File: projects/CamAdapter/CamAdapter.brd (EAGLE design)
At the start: 25.4 x 41.9 mm, 5 parts

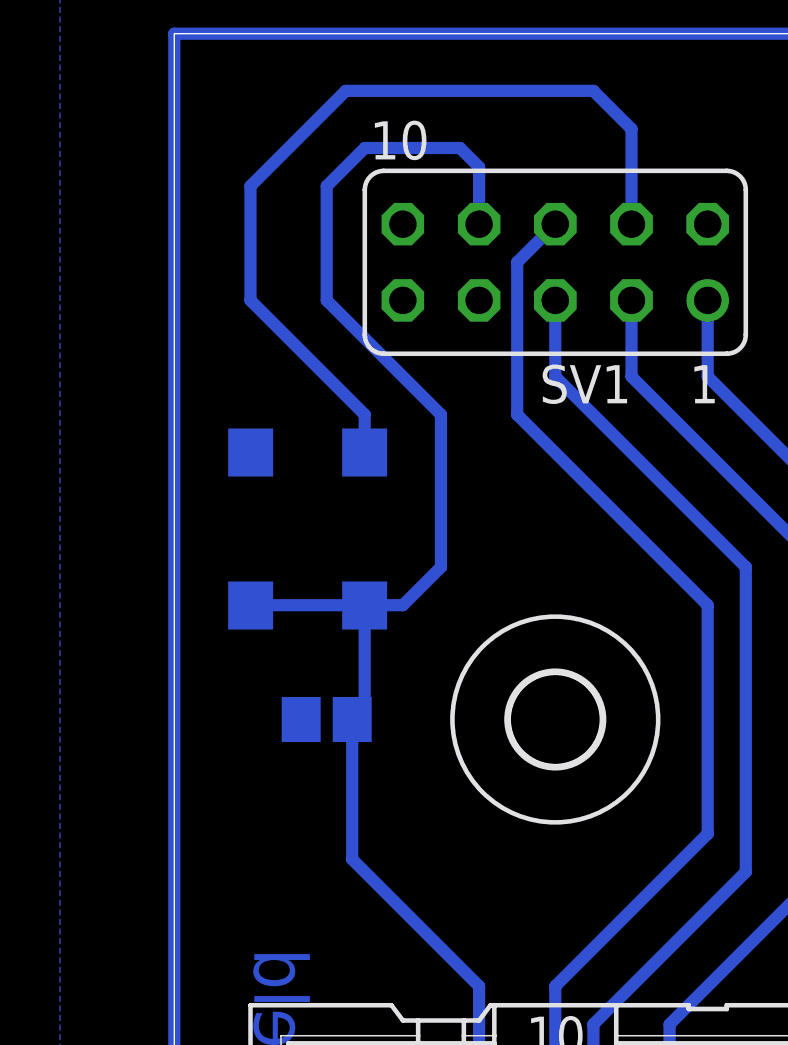
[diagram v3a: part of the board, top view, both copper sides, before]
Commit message: Enhaced space between signal trace and female pin header
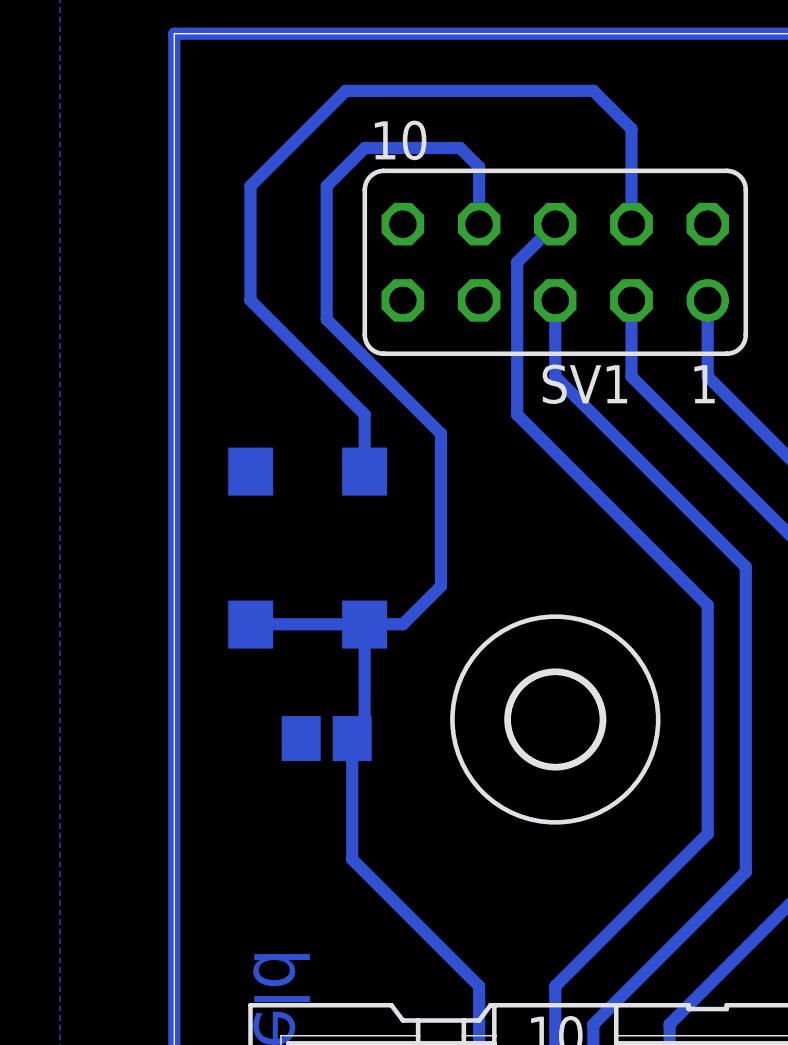
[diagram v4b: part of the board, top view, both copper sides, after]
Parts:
- moved C1 0.64 mm to (5.08, 18.4)
- moved QG1 0.63 mm to (4.45, 24.8)
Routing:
- net N$1: track 28.2 -> 28.8 mm
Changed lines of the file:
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@@
 </element>
 <element name="U$1" library="holes" package="3,0" value="" x="12.7" y="19.05"/>
-<element name="QG1" library="crystal" package="SM77H" value="SM77H" x="4.445" y="25.4" rot="MR90">
-<attribute name="OC_NEWARK" value="unknown" x="4.445" y="25.4" size="1.778" layer="28" rot="MR90" display="off"/>
-<attribute name="MPN" value="" x="4.445" y="25.4" size="1.778" layer="28" rot="MR90" display="off"/>
-<attribute name="MF" value="" x="4.445" y="25.4" size="1.778" layer="28" rot="MR90" display="off"/>
-<attribute name="OC_FARNELL" value="unknown" x="4.445" y="25.4" size="1.778" layer="28" rot="MR90" display="off"/>
+<element name="QG1" library="crystal" package="SM77H" value="SM77H" x="4.445" y="24.765" rot="MR90">
+<attribute name="OC_NEWARK" value="unknown" x="4.445" y="24.765" size="1.778" layer="28" rot="MR90" display="off"/>
+<attribute name="MPN" value="" x="4.445" y="24.765" size="1.778" layer="28" rot="MR90" display="off"/>
+<attribute name="MF" value="" x="4.445" y="24.765" size="1.778" layer="28" rot="MR90" display="off"/>
+<attribute name="OC_FARNELL" value="unknown" x="4.445" y="24.765" size="1.778" layer="28" rot="MR90" display="off"/>
 </element>
-<element name="C1" library="resistor" package="C0805" value="100n" x="5.08" y="19.05" rot="MR0"/>
+<element name="C1" library="resistor" package="C0805" value="100n" x="5.08" y="18.415" rot="MR0"/>
 </elements>
 <signals>
@@
 <contactref element="QG1" pad="4"/>
 <contactref element="C1" pad="1"/>
-<wire x1="6.355" y1="22.86" x2="6.345" y2="22.85" width="0.4064" layer="16"/>
-<wire x1="5.93" y1="19.05" x2="5.93" y2="14.39" width="0.4064" layer="16"/>
+<wire x1="6.355" y1="22.225" x2="6.345" y2="22.215" width="0.4064" layer="16"/>
+<wire x1="5.93" y1="18.415" x2="5.93" y2="14.39" width="0.4064" layer="16"/>
 <wire x1="5.93" y1="14.39" x2="10.16" y2="10.16" width="0.4064" layer="16"/>
 <wire x1="10.16" y1="10.16" x2="10.16" y2="6.35" width="0.4064" layer="16"/>
-<wire x1="6.345" y1="22.85" x2="6.345" y2="19.465" width="0.4064" layer="16"/>
-<wire x1="6.345" y1="19.465" x2="5.93" y2="19.05" width="0.4064" layer="16"/>
-<wire x1="6.355" y1="22.86" x2="7.62" y2="22.86" width="0.4064" layer="16"/>
-<wire x1="7.62" y1="22.86" x2="8.89" y2="24.13" width="0.4064" layer="16"/>
-<wire x1="8.89" y1="24.13" x2="8.89" y2="29.21" width="0.4064" layer="16"/>
-<wire x1="8.89" y1="29.21" x2="5.08" y2="33.02" width="0.4064" layer="16"/>
-<wire x1="5.08" y1="33.02" x2="5.08" y2="36.83" width="0.4064" layer="16"/>
+<wire x1="6.345" y1="22.215" x2="6.345" y2="18.83" width="0.4064" layer="16"/>
+<wire x1="6.345" y1="18.83" x2="5.93" y2="18.415" width="0.4064" layer="16"/>
+<wire x1="6.355" y1="22.225" x2="7.62" y2="22.225" width="0.4064" layer="16"/>
+<wire x1="7.62" y1="22.225" x2="8.89" y2="23.495" width="0.4064" layer="16"/>
+<wire x1="8.89" y1="23.495" x2="8.89" y2="28.575" width="0.4064" layer="16"/>
+<wire x1="8.89" y1="28.575" x2="5.08" y2="32.385" width="0.4064" layer="16"/>
+<wire x1="5.08" y1="32.385" x2="5.08" y2="36.83" width="0.4064" layer="16"/>
 <wire x1="5.08" y1="36.83" x2="6.35" y2="38.1" width="0.4064" layer="16"/>
 <wire x1="6.35" y1="38.1" x2="9.525" y2="38.1" width="0.4064" layer="16"/>
@@
 <wire x1="10.16" y1="37.465" x2="10.16" y2="35.56" width="0.4064" layer="16"/>
 <contactref element="QG1" pad="1"/>
-<wire x1="6.355" y1="22.86" x2="2.555" y2="22.86" width="0.4064" layer="16"/>
-<wire x1="2.555" y1="22.86" x2="2.545" y2="22.85" width="0.4064" layer="16"/>
+<wire x1="6.355" y1="22.225" x2="2.555" y2="22.225" width="0.4064" layer="16"/>
+<wire x1="2.555" y1="22.225" x2="2.545" y2="22.215" width="0.4064" layer="16"/>
 </signal>
 <signal name="N$1">
@@
 <wire x1="13.97" y1="40.005" x2="15.24" y2="38.735" width="0.4064" layer="16"/>
 <wire x1="15.24" y1="38.735" x2="15.24" y2="35.56" width="0.4064" layer="16"/>
-<wire x1="6.345" y1="27.95" x2="6.345" y2="29.215" width="0.4064" layer="16"/>
+<wire x1="6.345" y1="27.315" x2="6.345" y2="29.215" width="0.4064" layer="16"/>
 <wire x1="6.345" y1="29.215" x2="2.54" y2="33.02" width="0.4064" layer="16"/>
 <wire x1="2.54" y1="33.02" x2="2.54" y2="36.83" width="0.4064" layer="16"/>

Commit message: pcb2gcode outline & drill test
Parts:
- added JP1: (no value), pinhead:1X03
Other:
- outline, holes or cut-outs redrawn
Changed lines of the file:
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@@
 <board>
 <plain>
-<wire x1="0" y1="0" x2="25.4" y2="0" width="0" layer="20"/>
-<wire x1="25.4" y1="0" x2="25.4" y2="41.91" width="0" layer="20"/>
-<wire x1="25.4" y1="41.91" x2="0" y2="41.91" width="0" layer="20"/>
-<wire x1="0" y1="41.91" x2="0" y2="0" width="0" layer="20"/>
+<wire x1="0" y1="0" x2="25.4" y2="0" width="0.0254" layer="20"/>
+<wire x1="25.4" y1="0" x2="25.4" y2="40.64" width="0.0254" layer="20"/>
+<wire x1="25.4" y1="40.64" x2="24.13" y2="41.91" width="0.0254" layer="20"/>
+<wire x1="24.13" y1="41.91" x2="0" y2="41.91" width="0.0254" layer="20"/>
+<wire x1="0" y1="41.91" x2="0" y2="0" width="0.0254" layer="20"/>
 <text x="22.86" y="39.37" size="1.778" layer="16" font="vector" ratio="15" rot="MR270">cam</text>
 <text x="4.445" y="11.43" size="1.778" layer="16" font="vector" ratio="15" rot="MR270">shield</text>
@@
 </element>
 <element name="C1" library="resistor" package="C0805" value="100n" x="5.08" y="18.415" rot="MR0"/>
+<element name="JP1" library="pinhead" package="1X03" value="" x="22.86" y="30.48" rot="R90"/>
 </elements>
 <signals>
@@
 <contactref element="SV2" pad="9"/>
 <polygon width="0.4064" layer="16" isolate="0.3048">
-<vertex x="-3.81" y="45.72"/>
-<vertex x="31.75" y="45.72"/>
-<vertex x="31.75" y="-5.08"/>
-<vertex x="-3.81" y="-5.08"/>
+<vertex x="0" y="41.91"/>
+<vertex x="25.4" y="41.91"/>
+<vertex x="25.4" y="0"/>
+<vertex x="0" y="0"/>
 </polygon>
 <contactref element="SV1" pad="2"/>
@@
 <contactref element="QG1" pad="2"/>
 <contactref element="C1" pad="2"/>
+<wire x1="17.78" y1="6.35" x2="10.16" y2="3.81" width="0" layer="19" extent="1-1"/>
 </signal>
 <signal name="VCC">

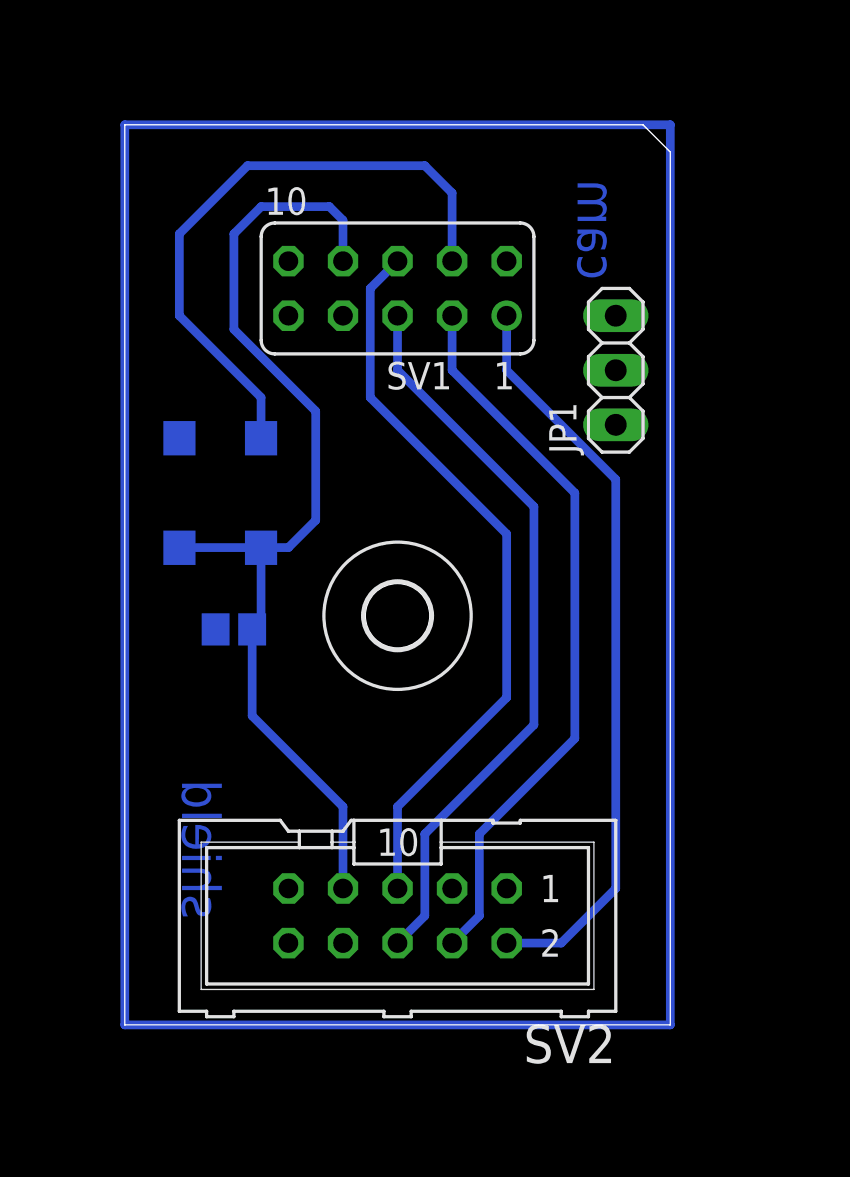
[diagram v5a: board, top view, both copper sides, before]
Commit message: Final
* finally found out pcb2gcode and CAM settings so that
  lower right corner is origin and coordinates relative to that point
	lign up when CNC milling
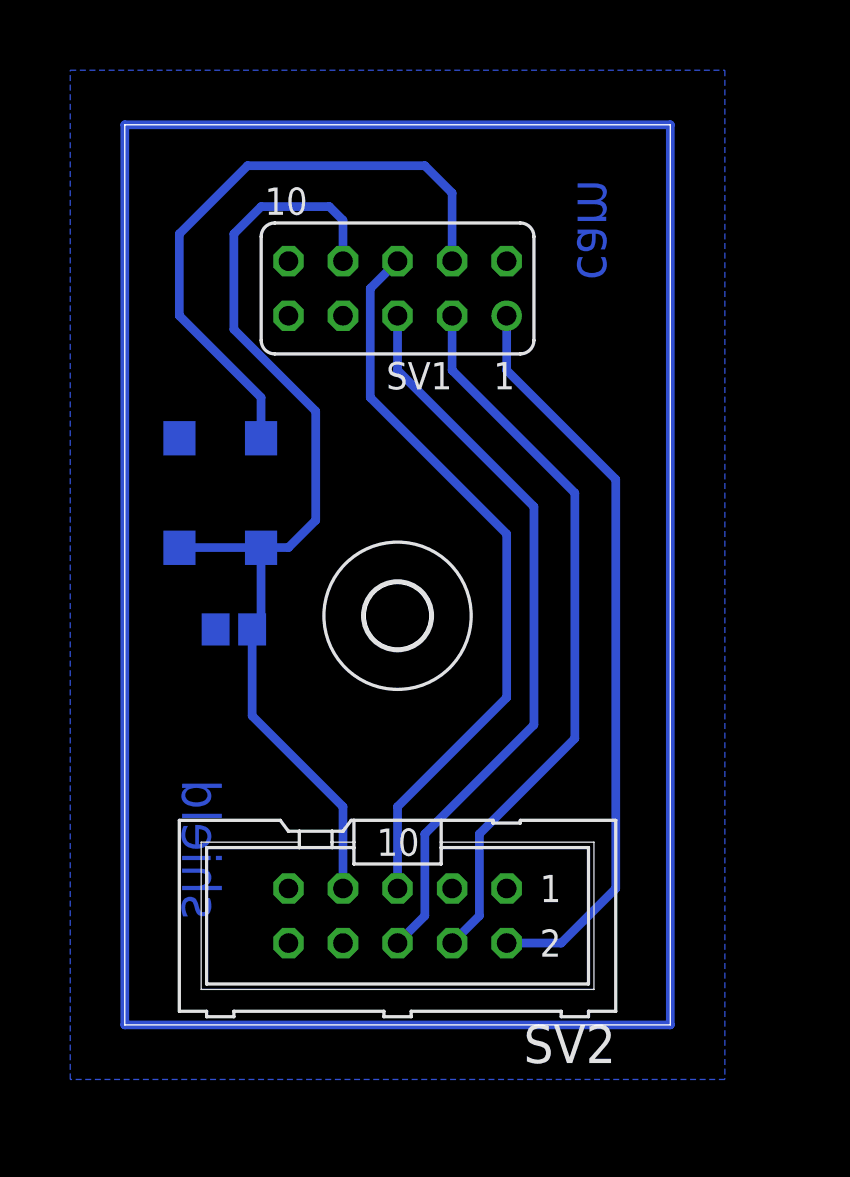
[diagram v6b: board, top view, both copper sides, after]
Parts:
- removed JP1: (no value), pinhead:1X03
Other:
- outline, holes or cut-outs redrawn
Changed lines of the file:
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@@
 <board>
 <plain>
-<wire x1="0" y1="0" x2="25.4" y2="0" width="0.0254" layer="20"/>
-<wire x1="25.4" y1="0" x2="25.4" y2="40.64" width="0.0254" layer="20"/>
-<wire x1="25.4" y1="40.64" x2="24.13" y2="41.91" width="0.0254" layer="20"/>
-<wire x1="24.13" y1="41.91" x2="0" y2="41.91" width="0.0254" layer="20"/>
-<wire x1="0" y1="41.91" x2="0" y2="0" width="0.0254" layer="20"/>
+<wire x1="0" y1="0" x2="25.4" y2="0" width="0.0508" layer="20"/>
+<wire x1="25.4" y1="0" x2="25.4" y2="41.91" width="0.0508" layer="20"/>
+<wire x1="25.4" y1="41.91" x2="0" y2="41.91" width="0.0508" layer="20"/>
+<wire x1="0" y1="41.91" x2="0" y2="0" width="0.0508" layer="20"/>
 <text x="22.86" y="39.37" size="1.778" layer="16" font="vector" ratio="15" rot="MR270">cam</text>
 <text x="4.445" y="11.43" size="1.778" layer="16" font="vector" ratio="15" rot="MR270">shield</text>
@@
 </element>
 <element name="C1" library="resistor" package="C0805" value="100n" x="5.08" y="18.415" rot="MR0"/>
-<element name="JP1" library="pinhead" package="1X03" value="" x="22.86" y="30.48" rot="R90"/>
 </elements>
 <signals>
@@
 <contactref element="SV2" pad="9"/>
 <polygon width="0.4064" layer="16" isolate="0.3048">
-<vertex x="0" y="41.91"/>
-<vertex x="25.4" y="41.91"/>
-<vertex x="25.4" y="0"/>
-<vertex x="0" y="0"/>
+<vertex x="-2.54" y="44.45"/>
+<vertex x="27.94" y="44.45"/>
+<vertex x="27.94" y="-2.54"/>
+<vertex x="-2.54" y="-2.54"/>
 </polygon>
 <contactref element="SV1" pad="2"/>
@@
 <contactref element="QG1" pad="2"/>
 <contactref element="C1" pad="2"/>
-<wire x1="17.78" y1="6.35" x2="10.16" y2="3.81" width="0" layer="19" extent="1-1"/>
 </signal>
 <signal name="VCC">
